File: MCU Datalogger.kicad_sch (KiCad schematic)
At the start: 0 parts

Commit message: Added some of the symbols.
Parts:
- added BT1: Battery, symbol Device:Battery
- added C1, C2, C3, C4: C, symbol Device:C
- added C5: C_Polarized, symbol Device:C_Polarized
- added D1, D2: LED, symbol Device:LED
- added H1, H2, H3, H4: MountingHole, symbol Mechanical:MountingHole
- added R1, R2, R3, R4, R5, R6, R7: R, symbol Device:R
- added U1, U2: 24LC1025, symbol Memory_EEPROM:24LC1025
- added Y1, Y2: Crystal, symbol Device:Crystal

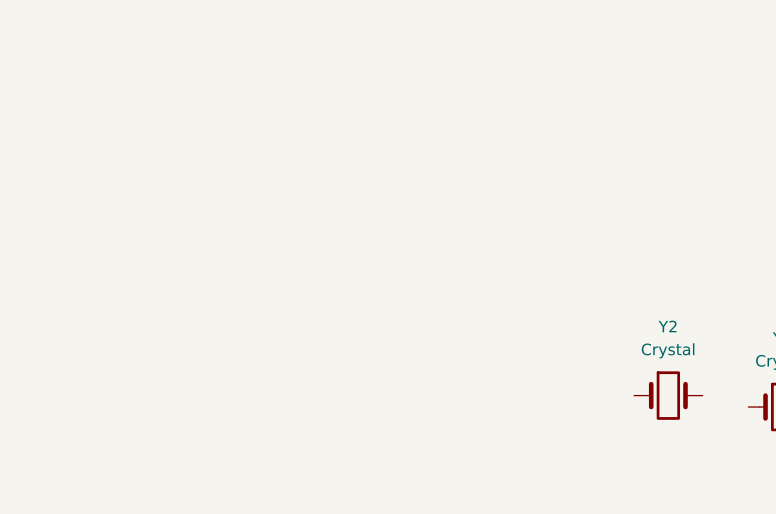
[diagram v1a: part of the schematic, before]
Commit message: Moved libraries to a local location.
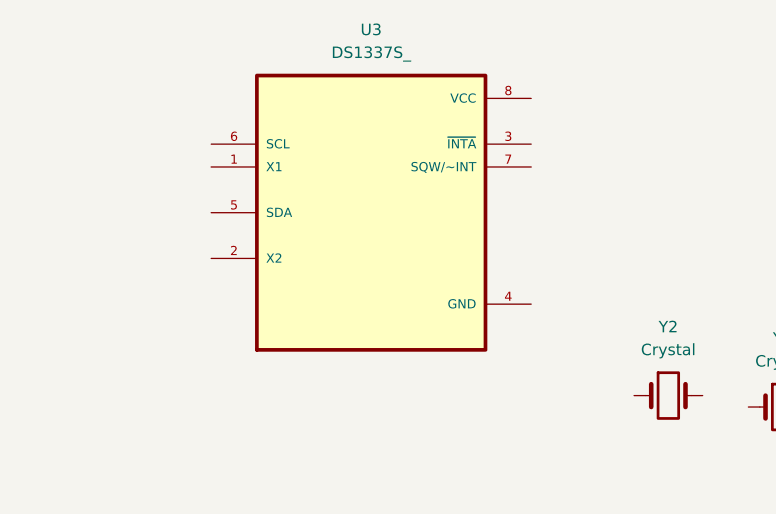
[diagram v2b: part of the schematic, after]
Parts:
- added U3: DS1337S_, Andreis sample library:SOIC127P600X175-8N, symbol DS1337S_:DS1337S_
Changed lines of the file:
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@@
+	)
+	(symbol
+		(lib_id "DS1337S_:DS1337S_")
+		(at 78.74 71.12 0)
+		(unit 1)
+		(exclude_from_sim no)
+		(in_bom yes)
+		(on_board yes)
+		(dnp no)
+		(fields_autoplaced yes)
+		(property "Reference" "U3"
+			(at 78.74 50.8 0)
+			(effects
+				(font
+					(size 1.27 1.27)
+				)
+			)
+		)
+		(property "Value" "DS1337S_"
+			(at 78.74 53.34 0)
+			(effects
+				(font
+					(size 1.27 1.27)
+				)
+			)
+		)
+		(property "Footprint" "Andreis sample library:SOIC127P600X175-8N"
+			(at 78.74 71.12 0)
+			(effects
+				(font
+					(size 1.27 1.27)
+				)
+				(justify bottom)
+				(hide yes)
+			)
+		)
+		(property "Datasheet" ""
+			(at 78.74 71.12 0)
+			(effects
+				(font
+					(size 1.27 1.27)
+				)
+				(hide yes)
+			)
+		)
+		(property "Description" ""
+			(at 78.74 71.12 0)
+			(effects
+				(font
+					(size 1.27 1.27)
+				)
+				(hide yes)
+			)
+		)
+		(property "MF" "Analog Devices"
+			(at 78.74 71.12 0)
+			(effects
+				(font
+					(size 1.27 1.27)
+				)
+				(justify bottom)
+				(hide yes)
+			)
+		)
+		(property "Description_1" "\n                        \n                            Real Time Clock (RTC) IC Clock/Calendar - I²C, 2-Wire Serial 8-SOIC (0.154, 3.90mm Width)\n                        \n"
+			(at 78.74 71.12 0)
+			(effects
+				(font
+					(size 1.27 1.27)
+				)
+				(justify bottom)
+				(hide yes)
+			)
+		)
+		(property "Package" "SOIC-8 Maxim"
+			(at 78.74 71.12 0)
+			(effects
+				(font
+					(size 1.27 1.27)
+				)
+				(justify bottom)
+				(hide yes)
+			)
+		)
+		(property "Price" "None"
+			(at 78.74 71.12 0)
+			(effects
+				(font
+					(size 1.27 1.27)
+				)
+				(justify bottom)
+				(hide yes)
+			)
+		)
+		(property "SnapEDA_Link" "https://www.snapeda.com/parts/DS1337S/Analog+Devices/view-part/?ref=snap"
+			(at 78.74 71.12 0)
+			(effects
+				(font
+					(size 1.27 1.27)
+				)
+				(justify bottom)
+				(hide yes)
+			)
+		)
+		(property "MP" "DS1337S"
+			(at 78.74 71.12 0)
+			(effects
+				(font
+					(size 1.27 1.27)
+				)
+				(justify bottom)
+				(hide yes)
+			)
+		)
+		(property "Availability" "In Stock"
+			(at 78.74 71.12 0)
+			(effects
+				(font
+					(size 1.27 1.27)
+				)
+				(justify bottom)
+				(hide yes)
+			)
+		)
+		(property "Check_prices" "https://www.snapeda.com/parts/DS1337S/Analog+Devices/view-part/?ref=eda"
+			(at 78.74 71.12 0)
+			(effects
+				(font
+					(size 1.27 1.27)
+				)
+				(justify bottom)
+				(hide yes)
+			)
+		)
+		(property "Purpose" ""
+			(at 78.74 71.12 0)
+			(effects
+				(font
+					(size 1.27 1.27)
+				)
+			)
+		)
+		(pin "1"
+		)
+		(pin "5"
+		)
+		(pin "7"
+		)
+		(pin "8"
+		)
+		(pin "6"
+		)
+		(pin "3"
+		)
+		(pin "2"
+		)
+		(pin "4"
+		)
+		(instances
+			(project ""
+				(path "/eb036d61-982e-41fc-ad07-0dff52d6a1cc"
+					(reference "U3")
+					(unit 1)
+				)
+			)
+		)
 	)
 	(symbol

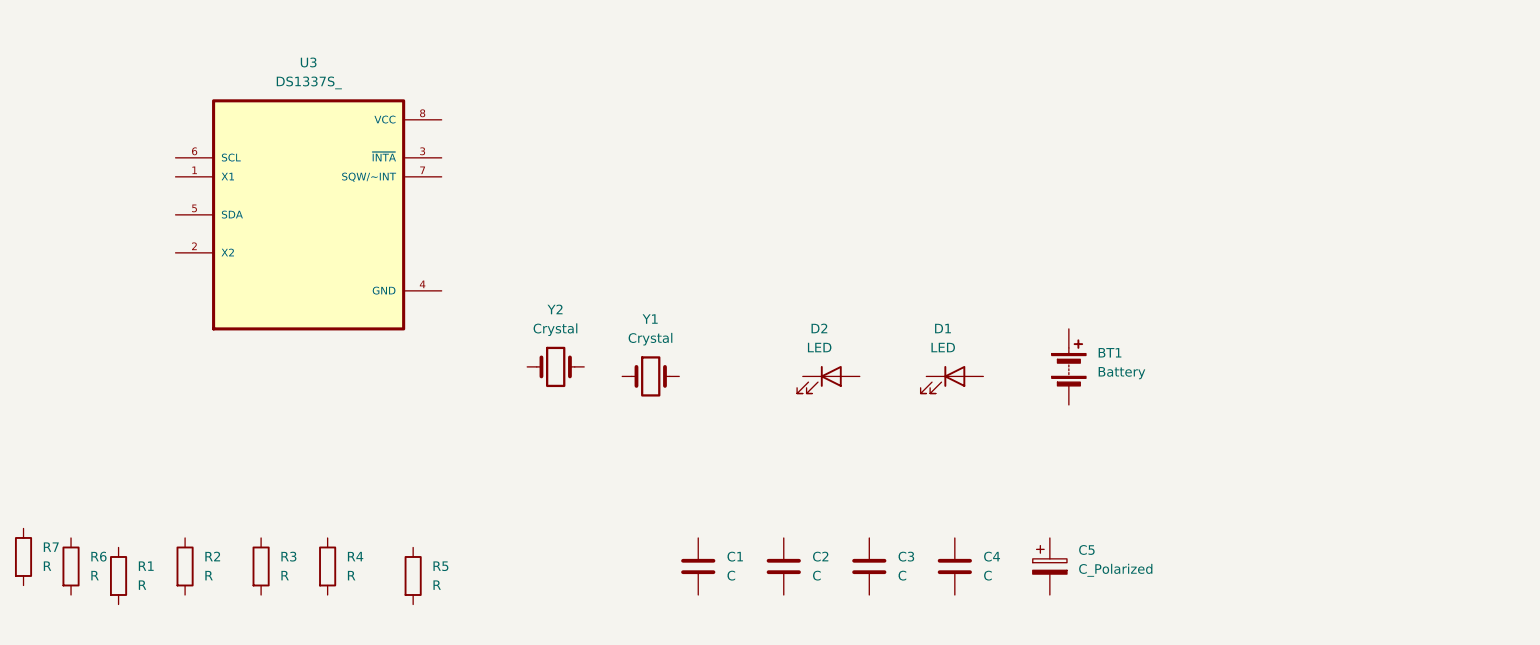
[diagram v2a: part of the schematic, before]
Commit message: Added DS1337S and ATMEGA328P-AU.
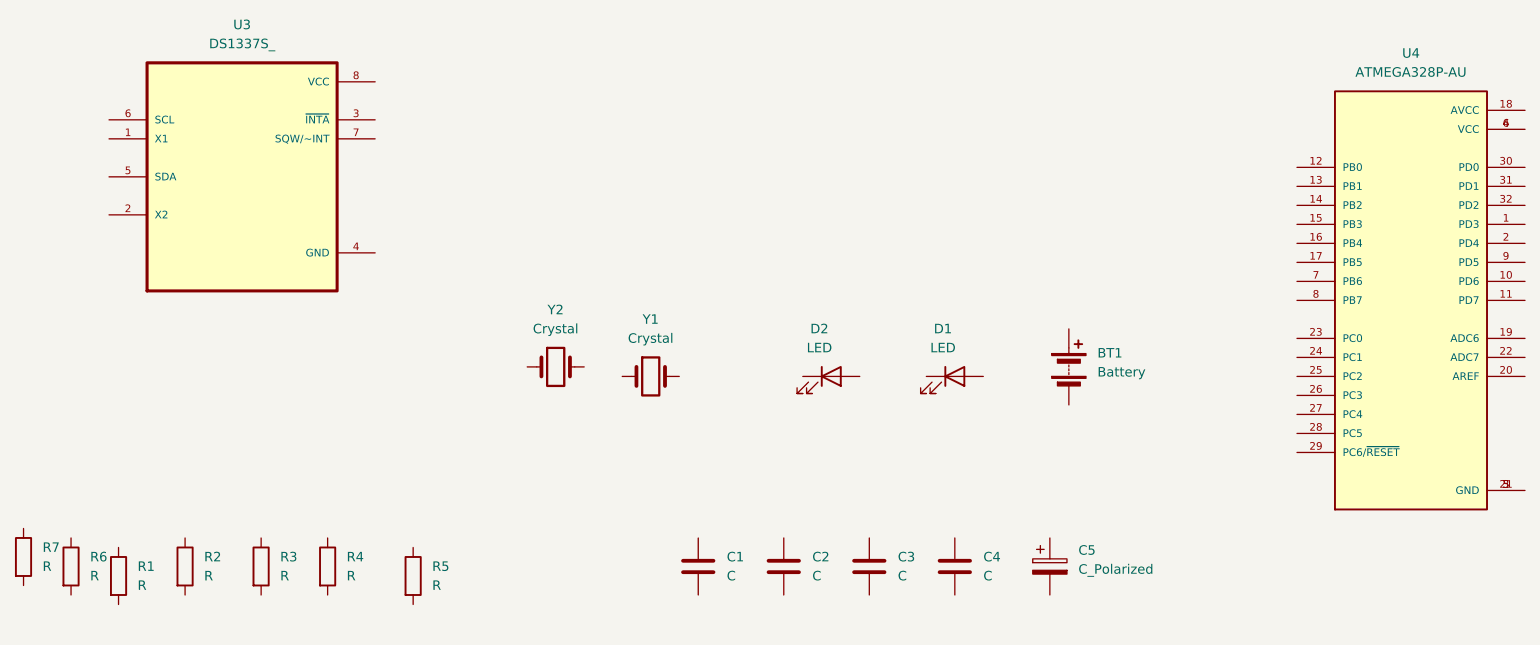
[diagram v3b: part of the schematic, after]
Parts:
- added U4: ATMEGA328P-AU, Andreis sample library:QFP80P900X900X120-32N, symbol ATMEGA328P-AU:ATMEGA328P-AU
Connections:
- new net: U4.21 (GND), U4.3 (GND), U4.5 (GND)
- new net: U4.4 (VCC), U4.6 (VCC)

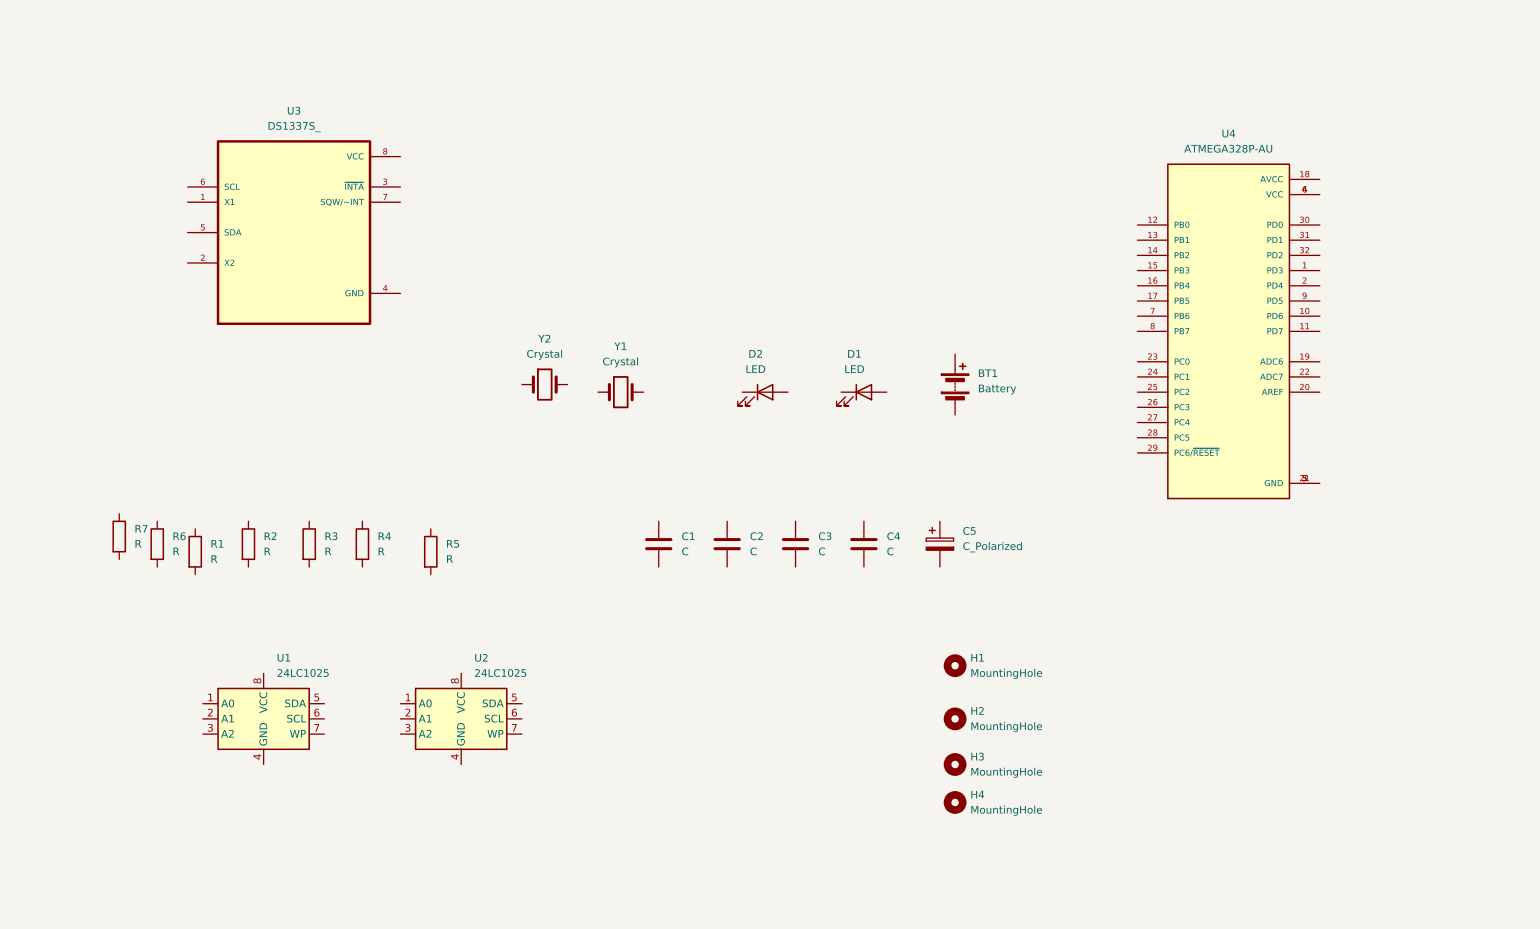
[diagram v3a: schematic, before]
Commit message: Created Libraries folder.
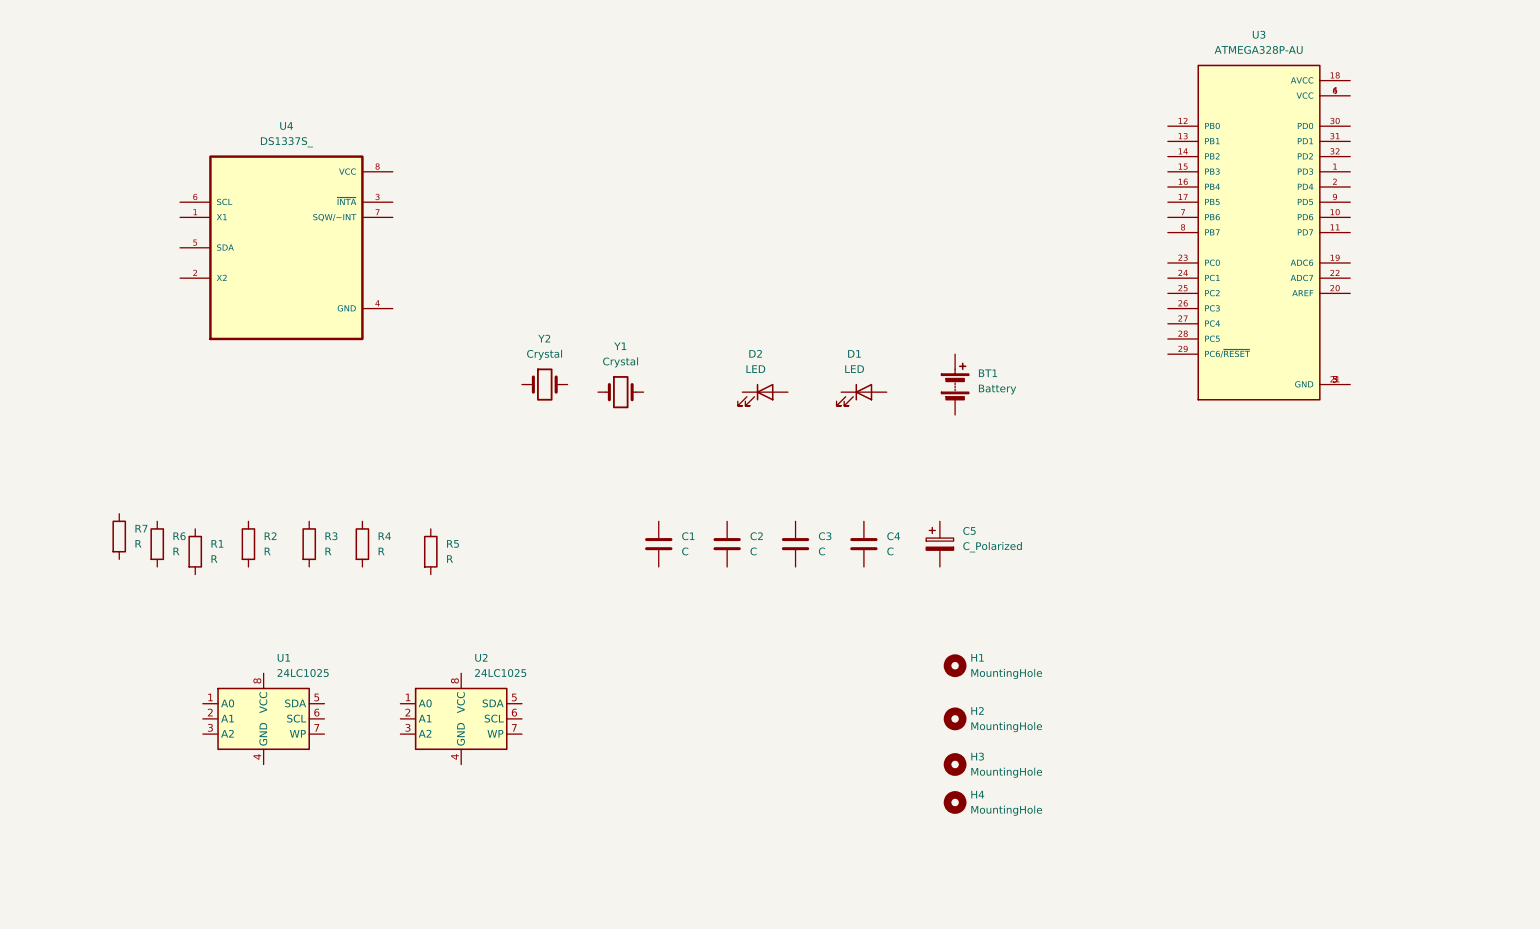
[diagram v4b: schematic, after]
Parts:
- removed U3: DS1337S_, Andreis sample library:SOIC127P600X175-8N, symbol DS1337S_:DS1337S_
- removed U4: ATMEGA328P-AU, Andreis sample library:QFP80P900X900X120-32N, symbol ATMEGA328P-AU:ATMEGA328P-AU
- added U3: ATMEGA328P-AU, ATMEGA328P-AU:QFP80P900X900X120-32N, symbol ATMEGA328P-AU:ATMEGA328P-AU
- added U4: DS1337S_, DS1337S_:SOIC127P600X175-8N, symbol DS1337S_:DS1337S_
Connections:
- new net: U3.21 (GND), U3.3 (GND), U3.5 (GND)
- new net: U3.4 (VCC), U3.6 (VCC)

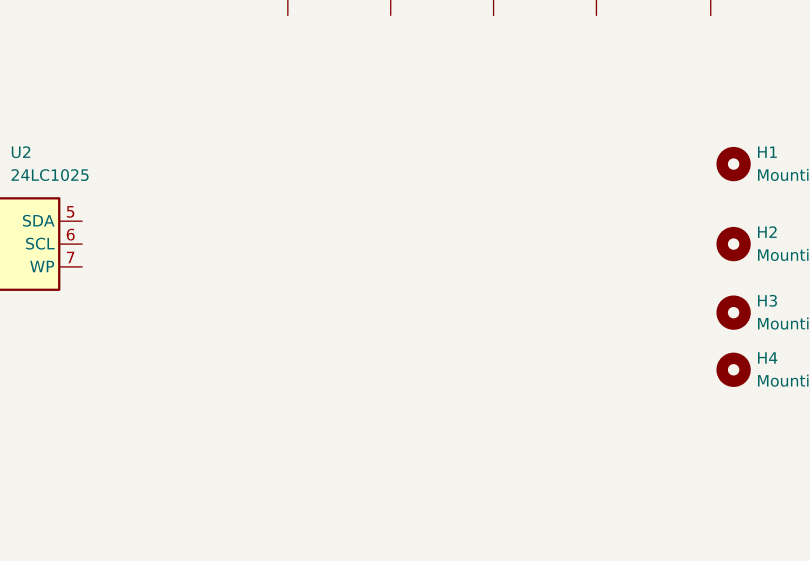
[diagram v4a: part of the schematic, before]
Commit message: Created a hierarchical sheet.
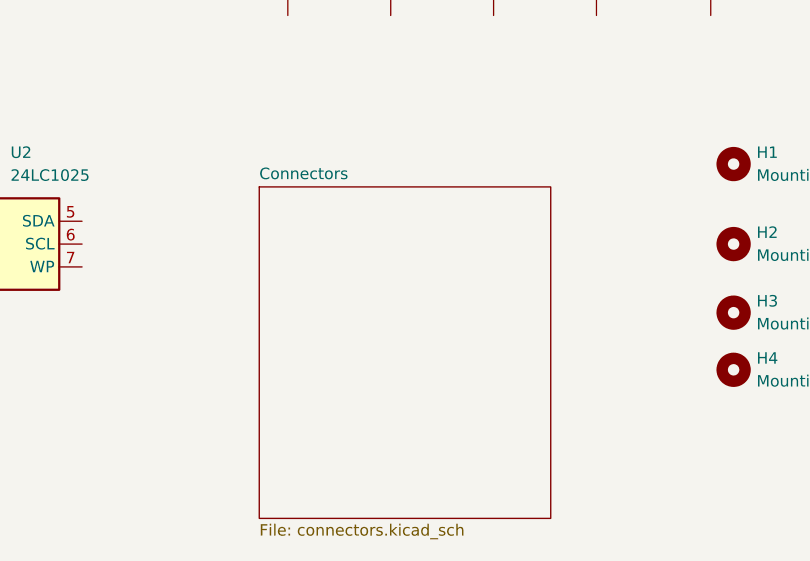
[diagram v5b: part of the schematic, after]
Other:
- added sheet Connectors (connectors.kicad_sch)
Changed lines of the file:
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@@
+		)
+	)
+	(sheet
+		(at 127.635 140.97)
+		(size 32.385 36.83)
+		(fields_autoplaced yes)
+		(stroke
+			(width 0.1524)
+			(type solid)
+		)
+		(fill
+			(color 0 0 0 0.0000)
+		)
+		(property "Sheetname" "Connectors"
+			(at 127.635 140.2584 0)
+			(effects
+				(font
+					(size 1.27 1.27)
+				)
+				(justify left bottom)
+			)
+		)
+		(property "Sheetfile" "connectors.kicad_sch"
+			(at 127.635 178.3846 0)
+			(effects
+				(font
+					(size 1.27 1.27)
+				)
+				(justify left top)
+			)
+		)
+		(instances
+			(project "MCU Datalogger"
+				(path "/eb036d61-982e-41fc-ad07-0dff52d6a1cc"
+					(page "2")
+				)
+			)
 		)
 	)
